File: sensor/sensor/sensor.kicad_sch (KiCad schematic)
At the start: 35 parts, among them J1 RJ12_Shielded, J2 Conn_01x04, J3 Conn_01x06, J8 RJ12_Shielded, J9 Conn_01x06, SW5 SW_Coded_SH-7050, U1 PCA9615DP, U2 LTC4316xDD, U5 TPS73101DBV

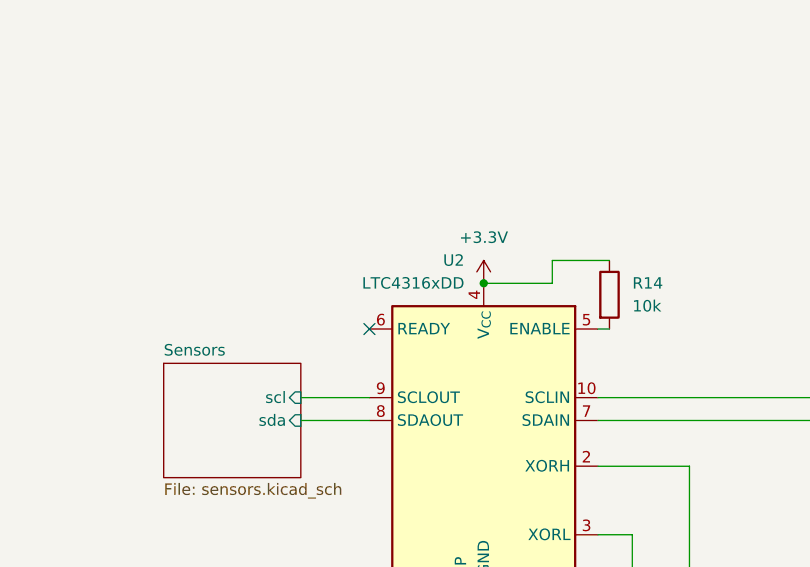
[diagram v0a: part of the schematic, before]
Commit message: Add BOM; Add LED; change LTC footprint
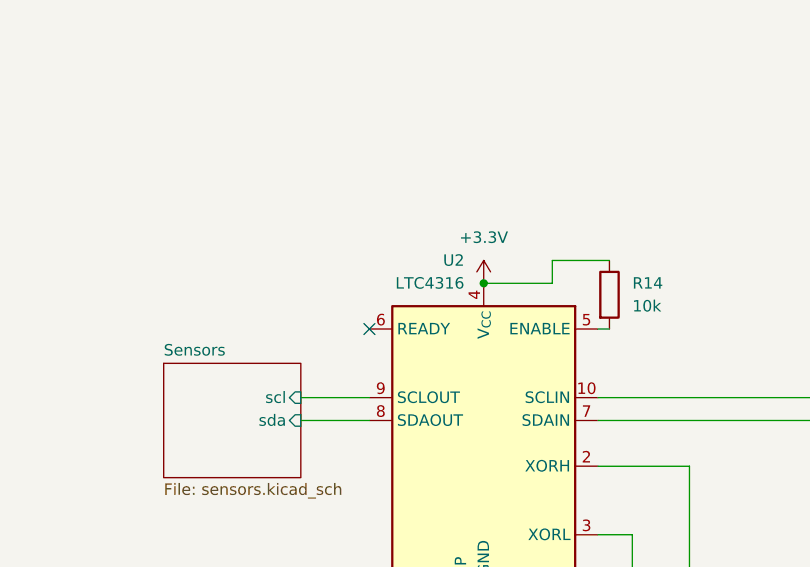
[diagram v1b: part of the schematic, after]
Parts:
- C1: Manufacturer_Part_Number 0402B102K500NT -> (none)
- C2, C3: Manufacturer_Part_Number CL10A105KB8NNNC -> (none)
- J1, J8: Supplier Name (none) -> LCSC; Supplier Part Number (none) -> C2683355; now in the parts list
- J2: Supplier Part Number (none) -> C51940130; now in the parts list
- J3, J9: Supplier Part Number (none) -> C160405; now in the parts list
- R1, R3, R4, R6: Manufacturer_Name (none) -> UNI-ROYAL(Uniroyal Elec); Manufacturer_Part_Number (none) -> 0402WGF6040TCE
- R10: Manufacturer_Name (none) -> UNI-ROYAL(Uniroyal Elec); Manufacturer_Part_Number (none) -> 0402WGF5102TCE; Substitution_Value (none) -> 51k
- R11: Manufacturer_Name (none) -> UNI-ROYAL(Uniroyal Elec); Manufacturer_Part_Number (none) -> 0402WGF3302TCE; Substitution_Value (none) -> 33k
- R12, R24: Manufacturer_Name (none) -> UNI-ROYAL(Uniroyal Elec); Manufacturer_Part_Number (none) -> 0402WGF4023TCE; Substitution_Value (none) -> 402k
- R13: Manufacturer_Name (none) -> UNI-ROYAL(Uniroyal Elec); Manufacturer_Part_Number (none) -> 0402WGF7503TCE
- R14, R26, R27, R9: Manufacturer_Name (none) -> UNI-ROYAL(Uniroyal Elec); Manufacturer_Part_Number (none) -> 0402WGF1002TCE
- R2, R5: Manufacturer_Name (none) -> UNI-ROYAL(Uniroyal Elec); Manufacturer_Part_Number (none) -> 0402WGF1200TCE
- R25: Manufacturer_Name (none) -> UNI-ROYAL(Uniroyal Elec); Manufacturer_Part_Number (none) -> 0402WGF7873TCE; Substitution_Value (none) -> 787k
- R28: Manufacturer_Name (none) -> UNI-ROYAL(Uniroyal Elec); Manufacturer_Part_Number (none) -> NQ02WGF8062TCE; Substitution_Value (none) -> 80.6k
- R29: Manufacturer_Name (none) -> UNI-ROYAL(Uniroyal Elec); Manufacturer_Part_Number (none) -> 0402WGF4022TCE; Substitution_Value (none) -> 40.2k
- R31: Manufacturer_Name (none) -> UNI-ROYAL(Uniroyal Elec); Manufacturer_Part_Number (none) -> 0402WGF2613TCE; Substitution_Value (none) -> 261k
- R7, R8: Manufacturer_Name (none) -> UNI-ROYAL(Uniroyal Elec); Manufacturer_Part_Number (none) -> 0402WGF4701TCE
- SW5: Manufacturer_Name (none) -> Khon; Manufacturer_Part_Number (none) -> ES07MP-16RBZ-L1500; Supplier Name (none) -> LCSC; now in the parts list
- U1: Manufacturer_Name (none) -> NXP; Supplier Name NXP -> Mouser/Digikey; now in the parts list
- U2: value LTC4316xDD -> LTC4316; footprint Package_DFN_QFN:DFN-10-1EP_3x3mm_P0.5mm_EP1.65x2.38mm -> Package_SO:MSOP-10_3x3mm_P0.5mm; Manufacturer_Name (none) -> Analog; Manufacturer_Part_Number (none) -> LTC4316xMS; Supplier Name JLCPCB -> Mouser/Digikey; now in the parts list
- U5: Manufacturer_Name (none) -> TI

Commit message: bom stuff
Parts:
- C1: JLCPCB Part (none) -> C1523
- C2, C3: JLCPCB Part (none) -> C15849
- J2: JLCPCB Part (none) -> C51940130
- J3, J9: JLCPCB Part (none) -> C160405
- R1, R3, R4, R6: JLCPCB Part (none) -> 0402WGF6040TCE
- R10: JLCPCB Part (none) -> 0402WGF5102TCE
- R11: JLCPCB Part (none) -> 0402WGF3302TCE
- R12, R24: JLCPCB Part (none) -> 0402WGF4023TCE
- R13: JLCPCB Part (none) -> 0402WGF7503TCE
- R14, R26, R27, R9: JLCPCB Part (none) -> 0402WGF1002TCE
- R2, R5: JLCPCB Part (none) -> 0402WGF1200TCE
- R25: JLCPCB Part (none) -> 0402WGF7873TCE
- R28: JLCPCB Part (none) -> NQ02WGF8062TCE
- R29: JLCPCB Part (none) -> 0402WGF4022TCE
- R31: JLCPCB Part (none) -> 0402WGF2613TCE
- R7, R8: JLCPCB Part (none) -> 0402WGF4701TCE
- U1: JLCPCB Part (none) -> PCA9615DP; Supplier Name Mouser/Digikey -> JLCPCB
- U2: JLCPCB Part (none) -> LTC4316xMS; Supplier Name Mouser/Digikey -> JLCPCB
- U5: JLCPCB Part (none) -> TPS73101DBV

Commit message: finished main sensor board
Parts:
- removed J1, J8: RJ12_Shielded, RJ12_Pin_Connector:RJ12_Pin_Connector, symbol Connector:RJ12_Shielded
- removed U2: LTC4316, Package_SO:MSOP-10_3x3mm_P0.5mm, symbol Interface_Expansion:LTC4316xDD
- added IC1: LTC4316CMS#TRPBF, LTC4316CMS:SOP50P490X110-10N, symbol LTC4316CMS#TRPBF:LTC4316CMS#TRPBF
- added J1, J6: GDLX-SMT-N-66, GDLX-SMT-N-66:GDLXSMTN66, symbol GDLX-SMT-N-66:GDLX-SMT-N-66
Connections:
- net +3.3V: now also R14.2, IC1.4 (VCC); no longer R14.1
- net +5V: now also J1.1, J6.1
- net GND: now also IC1.1 (GND), J1.6, J6.6
- net Sensors/scl: now also IC1.9 (SCLOUT)
- net Sensors/sda: now also IC1.8 (SDAOUT)
- net at J2.4 (Pin_4), R8.2, U1.4 (SCL): now also IC1.10 (SCLIN)
- net at R24.2, R25.2, R31.1: now also IC1.2 (XORH)
- net at R12.2, R13.2: now also IC1.3 (XORL)
- net at J2.3 (Pin_3), R7.2, U1.2 (SDA): now also IC1.7 (SDAIN)
- net at J3.2 (Pin_2), J9.2 (Pin_2), R1.2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: now also J1.2, J6.2
- net at J3.3 (Pin_3), J9.3 (Pin_3), R2.1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: now also J1.3, J6.3
- net at J3.4 (Pin_4), J9.4 (Pin_4), R4.2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: now also J1.4, J6.4
- net at J3.5 (Pin_5), J9.5 (Pin_5), R5.1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: now also J1.5, J6.5
- new net: IC1.5 (ENABLE), R14.1
- no-connect marks 3 -> 1
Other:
- moved on the sheet: R14

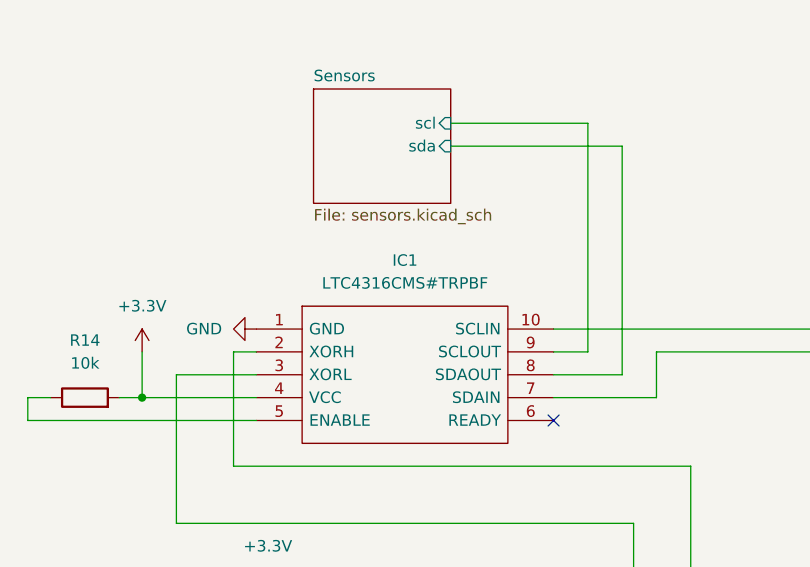
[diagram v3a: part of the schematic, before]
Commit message: add caps to host; make sensor_breakouts larger; update bom & generated production files for everything
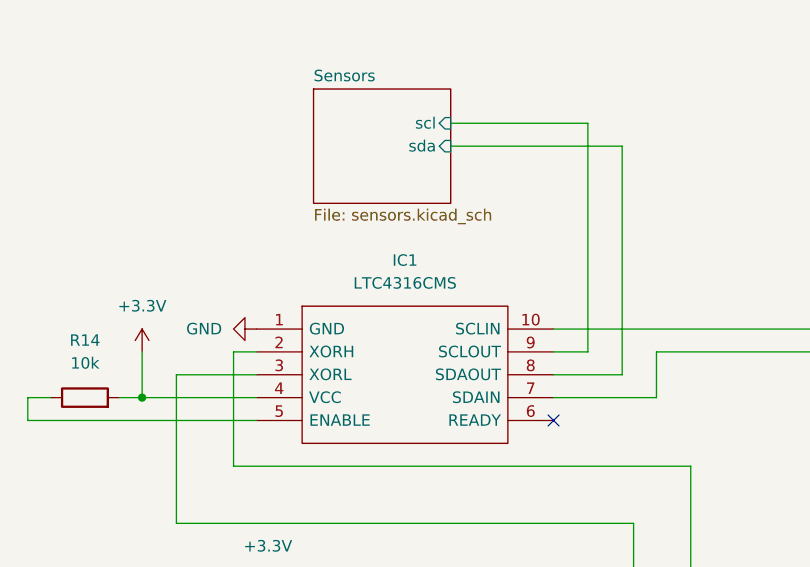
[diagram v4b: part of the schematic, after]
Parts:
- IC1: value LTC4316CMS#TRPBF -> LTC4316CMS
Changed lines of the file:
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@@
 			)
 		)
-		(property "Value" "LTC4316CMS#TRPBF"
+		(property "Value" "LTC4316CMS"
 			(at 69.85 69.85 0)
 			(effects
